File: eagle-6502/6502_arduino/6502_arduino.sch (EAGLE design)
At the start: 40 parts, among them U1 UM6507, U2 R6532, U3 28C256, U4 MCP2221-I/SL, U5 LFSPXO058610, U6 74HC00D, U7 74HC138D, X1 ARDUINO_UNO_PINS, X2 TACT_SWITCH, X3 TACT_SWITCH, X4 USB-B

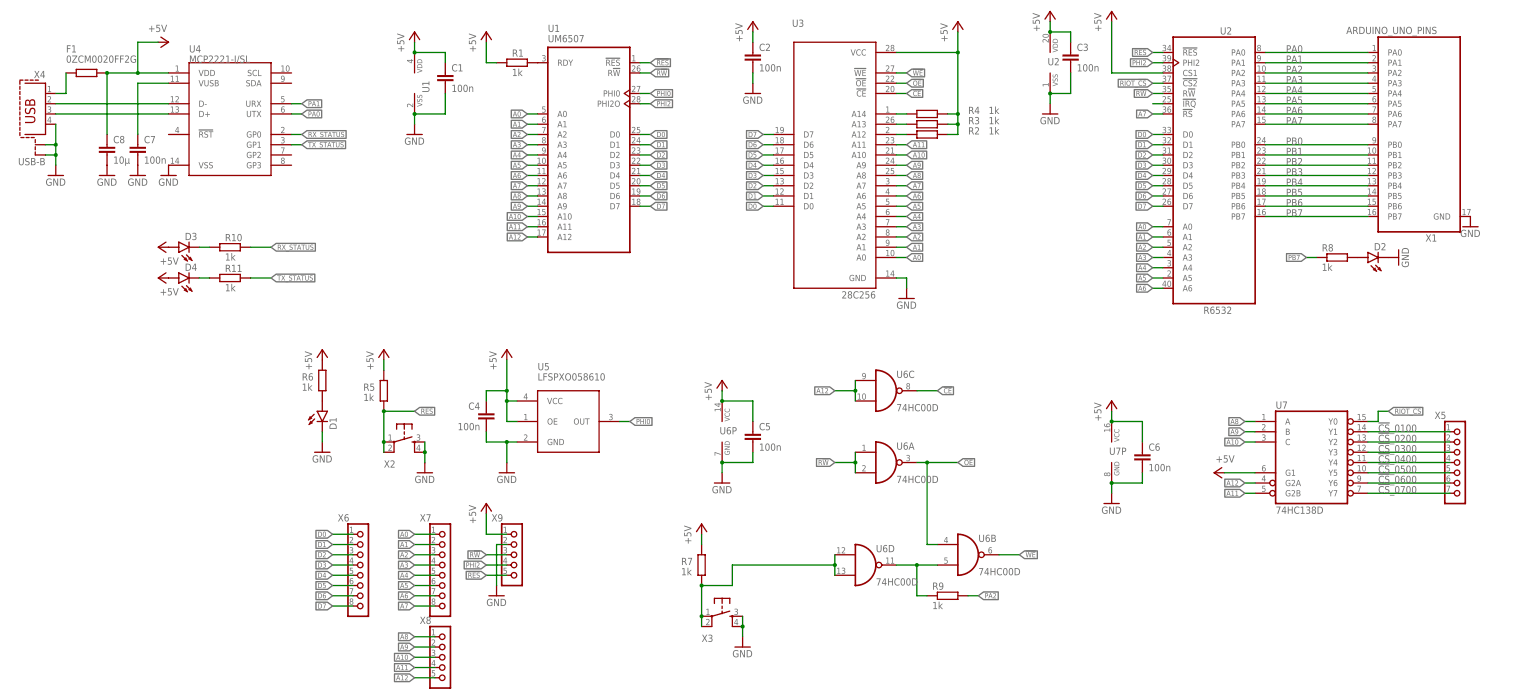
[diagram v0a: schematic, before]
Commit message: Tested PCB design on breadboard, added BAT54A ORing on 74x138 lines to allow stack served by RIOT, ORing of UART status LEDs
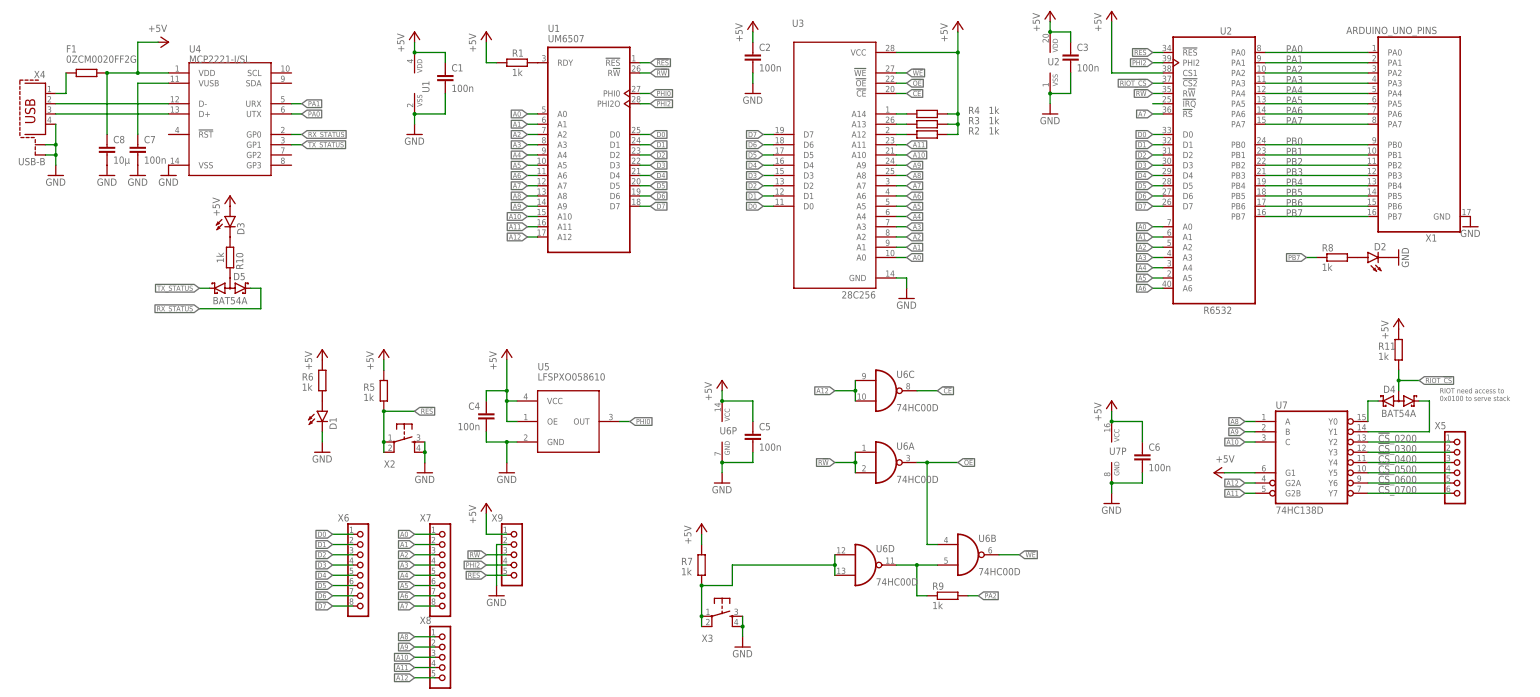
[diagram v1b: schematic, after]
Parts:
- added D5: BAT54A, diode:BAT54A
- D4: value (none) -> BAT54A; device 6502_lib:LED -> diode:BAT54A
- X5: device 6502_lib:PINHD_7_RND -> 6502_lib:PINHD_6_RND
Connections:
- removed net !CS!_0100: U7A.Y1, X5.1
- new net N$13: D4.K1, U7A.Y0
- new net N$17: D4.K2, U7A.Y1
- net !CS!_0200: now also X5.1; no longer X5.2
- net !CS!_0300: now also X5.2; no longer X5.3
- net !CS!_0400: now also X5.3; no longer X5.4
- net !CS!_0500: now also X5.4; no longer X5.5
- net !CS!_0600: now also X5.5; no longer X5.6
- net !CS!_0700: now also X5.6; no longer X5.7
- net +5V: now also R11.2; no longer D4.A
- net N$10: now also D5.AA, R10.2; no longer D4.C, R11.1
- net RIOT_!CS: now also D4.AA, R11.1; no longer U7A.Y0
- net RX_STATUS: now also D5.K2; no longer R10.2
- net TX_STATUS: now also D5.K1; no longer R11.2
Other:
- note added: "RIOT need access to 0x0100 to serve stack"
- moved on the sheet: D3, R10, R11
